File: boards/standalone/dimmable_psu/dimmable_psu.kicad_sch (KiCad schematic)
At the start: 51 parts

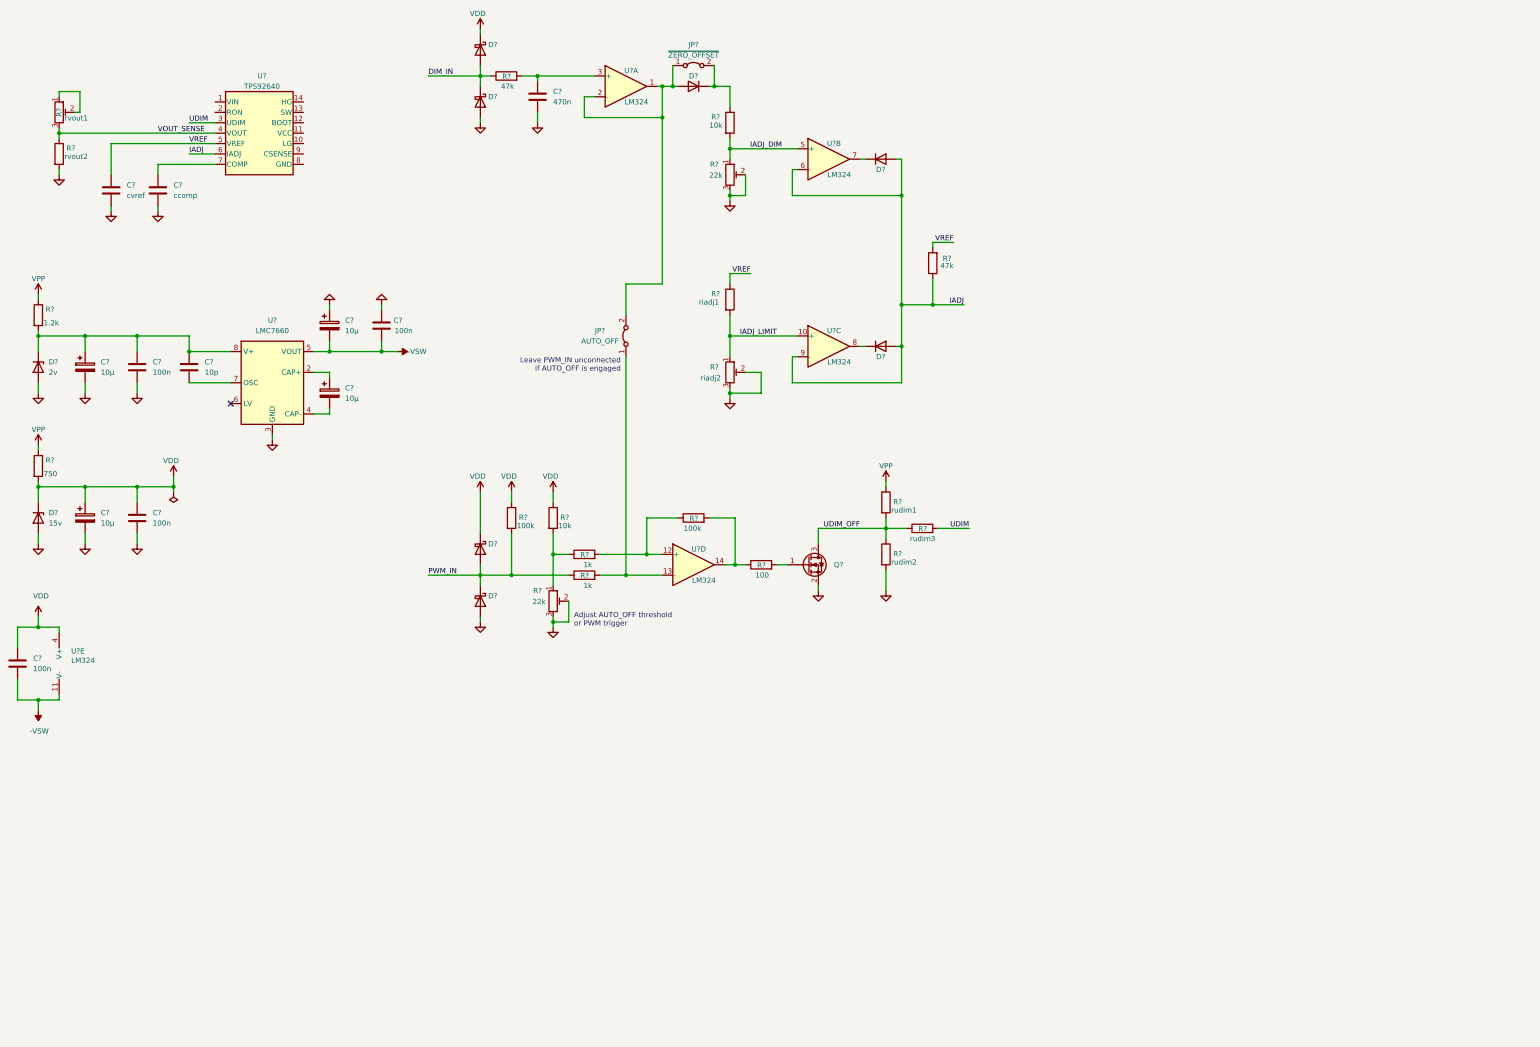
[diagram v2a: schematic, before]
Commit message: more or less a final version of the dimmable psu schematic
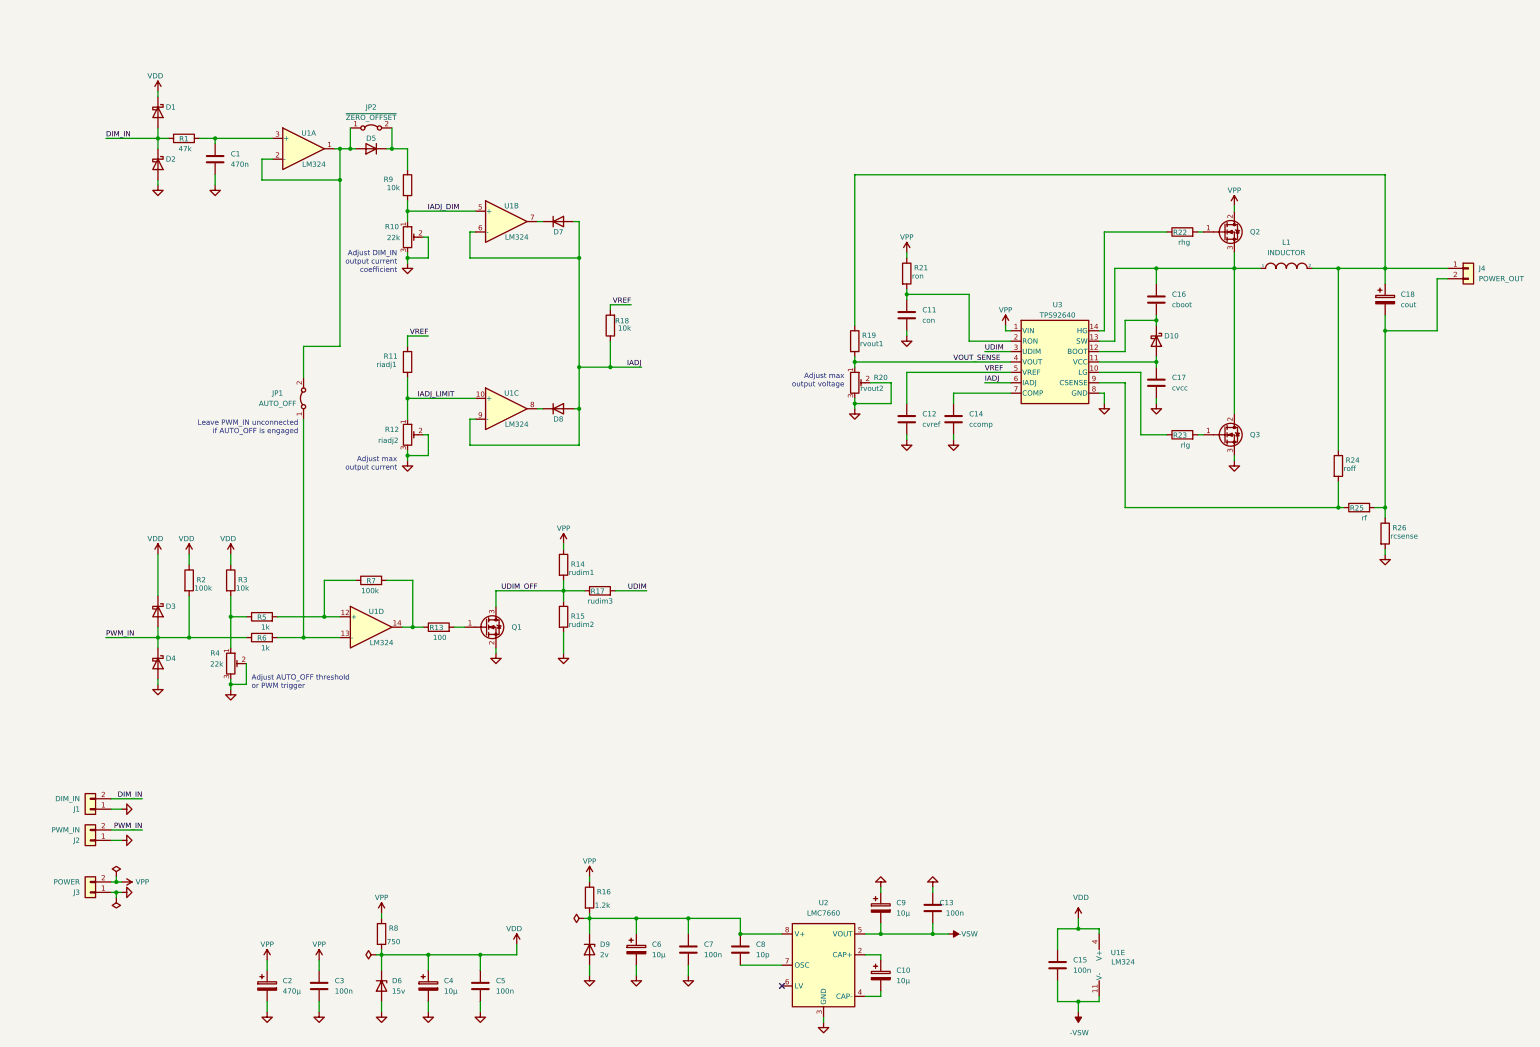
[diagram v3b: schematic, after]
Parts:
- added C11: con, Capacitor_SMD:C_0805_2012Metric_Pad1.18x1.45mm_HandSolder, symbol Device:C
- added C16: cboot, Capacitor_SMD:C_0805_2012Metric_Pad1.18x1.45mm_HandSolder, symbol Device:C
- added C17: cvcc, Capacitor_SMD:C_0805_2012Metric_Pad1.18x1.45mm_HandSolder, symbol Device:C
- added C18: cout, symbol Device:C_Polarized
- added C2: 470µ, symbol Device:C_Polarized
- added C3: 100n, Capacitor_SMD:C_0805_2012Metric_Pad1.18x1.45mm_HandSolder, symbol Device:C
- added D10: D_Schottky, symbol Device:D_Schottky
- added J1: DIM_IN, symbol Connector_Generic:Conn_01x02
- added J2: PWM_IN, symbol Connector_Generic:Conn_01x02
- added J3: POWER, symbol Connector_Generic:Conn_01x02
- added J4: POWER_OUT, symbol Connector_Generic:Conn_01x02
- added L1: INDUCTOR, symbol pspice:INDUCTOR
- added Q2, Q3: IRF540N, Package_TO_SOT_THT:TO-220-3_Vertical, symbol Transistor_FET:IRF540N
- added R21: ron, Resistor_SMD:R_0805_2012Metric_Pad1.20x1.40mm_HandSolder, symbol Device:R
- added R22: rhg, Resistor_SMD:R_0805_2012Metric_Pad1.20x1.40mm_HandSolder, symbol Device:R
- added R23: rlg, Resistor_SMD:R_0805_2012Metric_Pad1.20x1.40mm_HandSolder, symbol Device:R
- added R24: roff, symbol Device:R
- added R25: rf, Resistor_SMD:R_0805_2012Metric_Pad1.20x1.40mm_HandSolder, symbol Device:R
- added R26: rcsense, symbol Device:R
- R18: renamed from R?; value 47k -> 10k
- R19: renamed from R?; value rvout2 -> rvout1
- R20: renamed from R?; value rvout1 -> rvout2
- U2: renamed from U?; footprint (none) -> Package_SO:SOIC-8_3.9x4.9mm_P1.27mm
- gave numbers to parts that had none: 43
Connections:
- net DIM_IN: now also J1.2 (Pin_2)
- net GND: now also R20.2, R20.3, U3.8 (GND), C11.2, C17.2, C2.2, C3.2, J1.1 (Pin_1), J2.1 (Pin_1), J3.1 (Pin_1), Q3.3 (S), R26.2; no longer R19.2
- net PWM_IN: now also J2.2 (Pin_2)
- net VOUT_SENSE: now also R19.2, R20.1; no longer R19.1, R20.3
- net VPP: now also U3.1 (VIN), C2.1, C3.1, J3.2 (Pin_2), Q2.2 (D), R21.1
- net at U3.10 (LG): now also R23.1
- net at U3.11 (VCC): now also C17.1, D10.2 (A)
- net at U3.12 (BOOT): now also C16.2, D10.1 (K)
- net at U3.13 (SW): now also C16.1, L1.1, Q2.3 (S), Q3.2 (D)
- net at U3.14 (HG): now also R22.1
- net at U3.2 (RON): now also C11.1, R21.2
- net at U3.9 (CSENSE): now also R24.2, R25.1
- new net: Q3.1 (G), R23.2
- new net: C18.1, J4.1 (Pin_1), L1.2, R19.1, R24.1
- new net: Q2.1 (G), R22.2
- new net: C18.2, J4.2 (Pin_2), R25.2, R26.1
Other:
- note added: "Adjust DIM_IN output current coefficient"
- note added: "Adjust max output current"
- note added: "Adjust max output voltage"
- moved on the sheet: C1, C10, C12, C13, C14, C15, C4, C5, C6, C7, C8, C9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

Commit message: some more touches to dimmable_psu schematic
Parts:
- added R? (x2): 0.2, Resistor_THT:R_Axial_DIN0309_L9.0mm_D3.2mm_P12.70mm_Horizontal, symbol Device:R
- L1: value INDUCTOR -> 100µH; footprint (none) -> inductors:L_Bourns_SRR1770; shop (none) -> https://bg.farnell.com/bourns/srp1770ta-101m/inductor-100uh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
- R11: value riadj1 -> 10k
- R12: value riadj2 -> 22k
- R19: value rvout1 -> 150k
- R20: value rvout2 -> 22k
- R24: value roff -> 150; footprint (none) -> Resistor_THT:R_Axial_DIN0309_L9.0mm_D3.2mm_P12.70mm_Horizontal
- R25: value rf -> 10
- R26: value rcsense -> 0.2; footprint (none) -> Resistor_THT:R_Axial_DIN0309_L9.0mm_D3.2mm_P12.70mm_Horizontal
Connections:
- net GND: now also R?.2, R?.2
- net at C18.2, J4.2 (Pin_2), R25.2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: now also R?.1, R?.1
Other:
- note added: "ensures stability near zero"
- moved on the sheet: R24

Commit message: final touches to dimmable psu schematic
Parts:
- added R29: 10M, Resistor_SMD:R_0805_2012Metric_Pad1.20x1.40mm_HandSolder, symbol Device:R
- added TP1, TP2, TP3, TP4, TP5, TP6, TP7, TP8: TestPoint, TestPoint:TestPoint_THTPad_D2.0mm_Drill1.0mm, symbol Connector:TestPoint_Alt
- C10, C4, C6, C9: footprint (none) -> Capacitor_SMD:CP_Elec_5x5.4; shop (none) -> https://store.comet.bg/Catalogue/Product/29567/
- C11: value con -> 1n
- C12: value cvref -> 1µ
- C14: value ccomp -> 470n
- C16: value cboot -> 100n
- C17: value cvcc -> 2.2µ
- C18: value cout -> 100uF; footprint (none) -> Capacitor_THT:CP_Radial_D12.5mm_P5.00mm; shop (none) -> https://store.comet.bg/Catalogue/Product/29517/
- C2: footprint (none) -> Capacitor_THT:CP_Radial_D16.0mm_P7.50mm; shop (none) -> https://store.comet.bg/Catalogue/Product/29538/
- D1, D2, D3, D4: value D_Schottky -> D_Schottky_Trans; footprint (none) -> Diode_SMD:D_SOD-123
- D10: footprint (none) -> Diode_SMD:D_SOD-123
- D6: footprint Diode_SMD:D_SOD-123 -> Diode_THT:D_DO-15_P12.70mm_Horizontal
- D9: value 2v -> 2.7v; footprint Diode_SMD:D_SOD-123 -> Diode_THT:D_DO-15_P12.70mm_Horizontal
- J1, J2: footprint (none) -> wago:250-402
- J3, J4: footprint (none) -> wago:2061-602
- JP1, JP2: footprint (none) -> Connector_PinHeader_2.54mm:PinHeader_1x02_P2.54mm_Vertical
- R16, R25, R8: footprint Resistor_SMD:R_0805_2012Metric_Pad1.20x1.40mm_HandSolder -> Resistor_THT:R_Axial_DIN0309_L9.0mm_D3.2mm_P12.70mm_Horizontal
- gave numbers to parts that had none: 2
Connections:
- net -VSW: now also TP7.1
- net DIM_IN: now also R29.2
- net GND: now also U2.6 (LV)
- net IADJ: now also TP5.1
- net IADJ_DIM: now also TP2.1
- net IADJ_LIMIT: now also TP3.1
- net UDIM: now also TP6.1
- net VDD: now also R29.1, TP4.1
- net at C16.1, L1.1, Q2.3 (S)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: now also TP8.1
- net at R13.1, R7.2, U1.14: now also TP1.1
- no-connect marks 1 -> 0
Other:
- moved on the sheet: D1, D2

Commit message: proper footprint for opamp
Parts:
- U1: footprint Package_SO:SO-14_3.9x8.65mm_P1.27mm -> Package_SO:SOIC-14_3.9x8.7mm_P1.27mm
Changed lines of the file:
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@@
     (property "Reference" "U1" (id 0) (at 294.132 244.602 0))
     (property "Value" "LM324" (id 1) (at 295.402 246.888 0))
-    (property "Footprint" "Package_SO:SO-14_3.9x8.65mm_P1.27mm" (id 2) (at 290.83 245.11 0)
+    (property "Footprint" "Package_SO:SOIC-14_3.9x8.7mm_P1.27mm" (id 2) (at 290.83 245.11 0)
       (effects (font (size 1.27 1.27)) hide)
     )
@@
     (property "Reference" "U1" (id 0) (at 96.52 44.45 0))
     (property "Value" "LM324" (id 1) (at 97.79 52.07 0))
-    (property "Footprint" "Package_SO:SO-14_3.9x8.65mm_P1.27mm" (id 2) (at 93.98 45.72 0)
+    (property "Footprint" "Package_SO:SOIC-14_3.9x8.7mm_P1.27mm" (id 2) (at 93.98 45.72 0)
       (effects (font (size 1.27 1.27)) hide)
     )
@@
     (property "Reference" "U1" (id 0) (at 113.03 161.29 0))
     (property "Value" "LM324" (id 1) (at 114.3 168.91 0))
-    (property "Footprint" "Package_SO:SO-14_3.9x8.65mm_P1.27mm" (id 2) (at 110.49 162.56 0)
+    (property "Footprint" "Package_SO:SOIC-14_3.9x8.7mm_P1.27mm" (id 2) (at 110.49 162.56 0)
       (effects (font (size 1.27 1.27)) hide)
     )
@@
     (property "Reference" "U1" (id 0) (at 146.05 62.23 0))
     (property "Value" "LM324" (id 1) (at 147.32 69.85 0))
-    (property "Footprint" "Package_SO:SO-14_3.9x8.65mm_P1.27mm" (id 2) (at 143.51 63.5 0)
+    (property "Footprint" "Package_SO:SOIC-14_3.9x8.7mm_P1.27mm" (id 2) (at 143.51 63.5 0)
       (effects (font (size 1.27 1.27)) hide)
     )
@@
     (property "Reference" "U1" (id 0) (at 146.05 107.95 0))
     (property "Value" "LM324" (id 1) (at 147.32 115.57 0))
-    (property "Footprint" "Package_SO:SO-14_3.9x8.65mm_P1.27mm" (id 2) (at 143.51 109.22 0)
+    (property "Footprint" "Package_SO:SOIC-14_3.9x8.7mm_P1.27mm" (id 2) (at 143.51 109.22 0)
       (effects (font (size 1.27 1.27)) hide)
     )
@@
     )
     (path "/ced8a113-f45f-473d-93c2-d1cc90639fc7"
-      (reference "U1") (unit 1) (value "LM324") (footprint "Package_SO:SO-14_3.9x8.65mm_P1.27mm")
+      (reference "U1") (unit 1) (value "LM324") (footprint "Package_SO:SOIC-14_3.9x8.7mm_P1.27mm")
     )
     (path "/5bba5587-e7bf-41e8-b018-e73eb1f7dfe2"
-      (reference "U1") (unit 2) (value "LM324") (footprint "Package_SO:SO-14_3.9x8.65mm_P1.27mm")
+      (reference "U1") (unit 2) (value "LM324") (footprint "Package_SO:SOIC-14_3.9x8.7mm_P1.27mm")
     )
     (path "/7d276db1-487e-4bb5-9264-c4ab165985c9"
-      (reference "U1") (unit 3) (value "LM324") (footprint "Package_SO:SO-14_3.9x8.65mm_P1.27mm")
+      (reference "U1") (unit 3) (value "LM324") (footprint "Package_SO:SOIC-14_3.9x8.7mm_P1.27mm")
     )
     (path "/151f3ea5-ae39-47c5-8308-d706d300d116"
-      (reference "U1") (unit 4) (value "LM324") (footprint "Package_SO:SO-14_3.9x8.65mm_P1.27mm")
+      (reference "U1") (unit 4) (value "LM324") (footprint "Package_SO:SOIC-14_3.9x8.7mm_P1.27mm")
     )
     (path "/bd7742d1-ac9a-4cac-9b1d-4b62d4bd2039"
-      (reference "U1") (unit 5) (value "LM324") (footprint "Package_SO:SO-14_3.9x8.65mm_P1.27mm")
+      (reference "U1") (unit 5) (value "LM324") (footprint "Package_SO:SOIC-14_3.9x8.7mm_P1.27mm")
     )
     (path "/07bae109-7890-4c91-8570-aabec3d6db7f"

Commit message: mounting holes!
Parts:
- added H? (x4): MountingHole_Pad, MountingHole:MountingHole_3.2mm_M3_Pad, symbol Mechanical:MountingHole_Pad
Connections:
- no-connect marks 0 -> 4
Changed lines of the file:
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@@
   (junction (at 359.41 135.89) (diameter 1.016) (color 0 0 0 0))
   (junction (at 368.3 135.89) (diameter 1.016) (color 0 0 0 0))
+  (no_connect (at 372.745 258.445))
+  (no_connect (at 377.19 258.445))
+  (no_connect (at 381.635 258.445))
+  (no_connect (at 386.08 258.445))
   (wire (pts (xy 39.37 45.72) (xy 52.07 45.72))
     (stroke (width 0) (type solid) (color 0 0 0 0))
@@
     (pin "2")
   )
+  (symbol (lib_id "Mechanical:MountingHole_Pad") (at 372.745 255.905 0) (unit 1)
+    (in_bom yes) (on_board yes)
+    (property "Reference" "H?" (id 0) (at 371.475 251.46 0)
+      (effects (font (size 1.27 1.27)) (justify left))
+    )
+    (property "Value" "MountingHole_Pad" (id 1) (at 375.92 257.81 0)
+      (effects (font (size 1.27 1.27)) (justify left) hide)
+    )
+    (property "Footprint" "MountingHole:MountingHole_3.2mm_M3_Pad" (id 2) (at 372.745 255.905 0)
+      (effects (font (size 1.27 1.27)) hide)
+    )
+    (property "Datasheet" "~" (id 3) (at 372.745 255.905 0)
+      (effects (font (size 1.27 1.27)) hide)
+    )
+    (pin "1")
+  )
+  (symbol (lib_id "Mechanical:MountingHole_Pad") (at 377.19 255.905 0) (unit 1)
+    (in_bom yes) (on_board yes)
+    (property "Reference" "H?" (id 0) (at 375.92 251.46 0)
+      (effects (font (size 1.27 1.27)) (justify left))
+    )
+    (property "Value" "MountingHole_Pad" (id 1) (at 380.365 257.81 0)
+      (effects (font (size 1.27 1.27)) (justify left) hide)
+    )
+    (property "Footprint" "MountingHole:MountingHole_3.2mm_M3_Pad" (id 2) (at 377.19 255.905 0)
+      (effects (font (size 1.27 1.27)) hide)
+    )
+    (property "Datasheet" "~" (id 3) (at 377.19 255.905 0)
+      (effects (font (size 1.27 1.27)) hide)
+    )
+    (pin "1")
+  )
+  (symbol (lib_id "Mechanical:MountingHole_Pad") (at 381.635 255.905 0) (unit 1)
+    (in_bom yes) (on_board yes)
+    (property "Reference" "H?" (id 0) (at 380.365 251.46 0)
+      (effects (font (size 1.27 1.27)) (justify left))
+    )
+    (property "Value" "MountingHole_Pad" (id 1) (at 384.81 257.81 0)
+      (effects (font (size 1.27 1.27)) (justify left) hide)
+    )
+    (property "Footprint" "MountingHole:MountingHole_3.2mm_M3_Pad" (id 2) (at 381.635 255.905 0)
+      (effects (font (size 1.27 1.27)) hide)
+    )
+    (property "Datasheet" "~" (id 3) (at 381.635 255.905 0)
+      (effects (font (size 1.27 1.27)) hide)
+    )
+    (pin "1")
+  )
+  (symbol (lib_id "Mechanical:MountingHole_Pad") (at 386.08 255.905 0) (unit 1)
+    (in_bom yes) (on_board yes)
+    (property "Reference" "H?" (id 0) (at 384.81 251.46 0)
+      (effects (font (size 1.27 1.27)) (justify left))
+    )
+    (property "Value" "MountingHole_Pad" (id 1) (at 389.255 257.81 0)
+      (effects (font (size 1.27 1.27)) (justify left) hide)
+    )
+    (property "Footprint" "MountingHole:MountingHole_3.2mm_M3_Pad" (id 2) (at 386.08 255.905 0)
+      (effects (font (size 1.27 1.27)) hide)
+    )
+    (property "Datasheet" "~" (id 3) (at 386.08 255.905 0)
+      (effects (font (size 1.27 1.27)) hide)
+    )
+    (pin "1")
+  )
   (symbol (lib_id "Device:D_Schottky") (at 52.07 39.37 270) (unit 1)
     (in_bom yes) (on_board yes)
@@
       (reference "D10") (unit 1) (value "D_Schottky") (footprint "Diode_SMD:D_SOD-123")
     )
+    (path "/023ebd38-5f1e-458e-be61-bb156e5173ae"
+      (reference "H?") (unit 1) (value "MountingHole_Pad") (footprint "MountingHole:MountingHole_3.2mm_M3_Pad")
+    )
+    (path "/18a07627-8ae3-4b6b-89bb-064a36bbb40d"
+      (reference "H?") (unit 1) (value "MountingHole_Pad") (footprint "MountingHole:MountingHole_3.2mm_M3_Pad")
+    )
+    (path "/dc36ab86-8ce5-42ab-87c0-719642f09dff"
+      (reference "H?") (unit 1) (value "MountingHole_Pad") (footprint "MountingHole:MountingHole_3.2mm_M3_Pad")
+    )
+    (path "/edab61e6-910c-4e8e-95df-adcb0437978a"
+      (reference "H?") (unit 1) (value "MountingHole_Pad") (footprint "MountingHole:MountingHole_3.2mm_M3_Pad")
+    )
     (path "/d48847fd-ac00-4036-90e4-501d8884232c"
